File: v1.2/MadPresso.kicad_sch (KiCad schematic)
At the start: 42 parts, among them J1 Conn_01x07, J2 Conn_01x03, J3 Conn_01x02, J4 Conn_01x04, Q1 BC847, Q2 BSS84, U1 LTV-356T, U2 ADC101C021CIMK, U3 WeMos_D1_mini

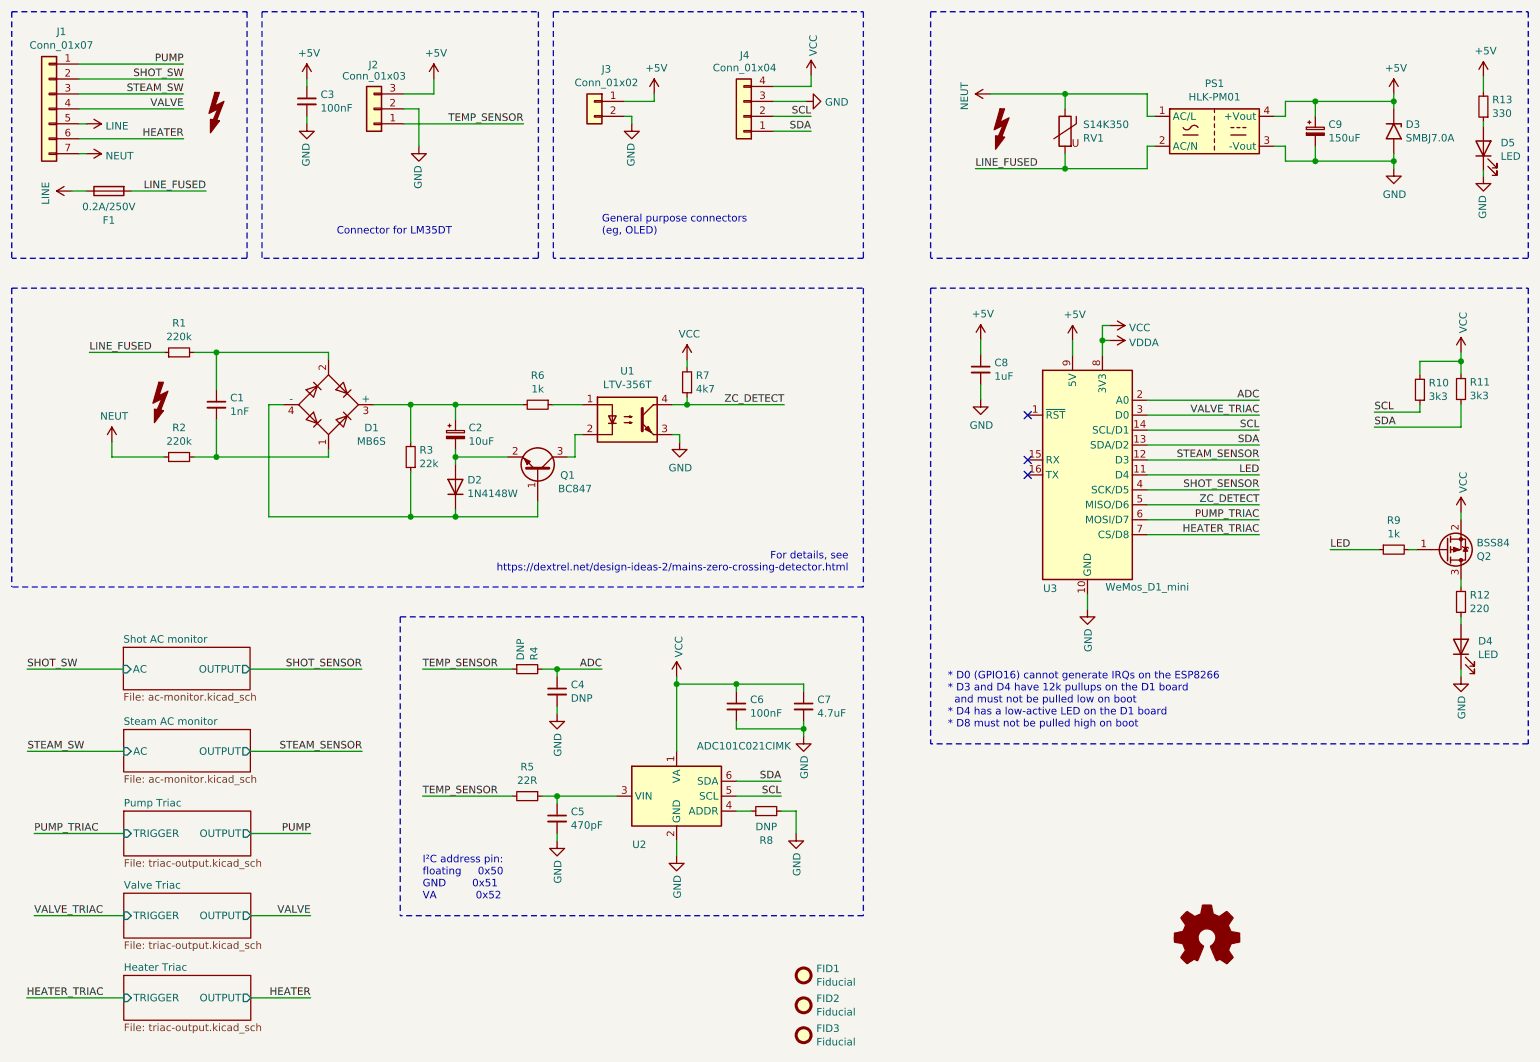
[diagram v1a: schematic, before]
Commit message: More updates
* make pump triac switch NEUT, not LINE
* move ADC a bit
* improve clearance
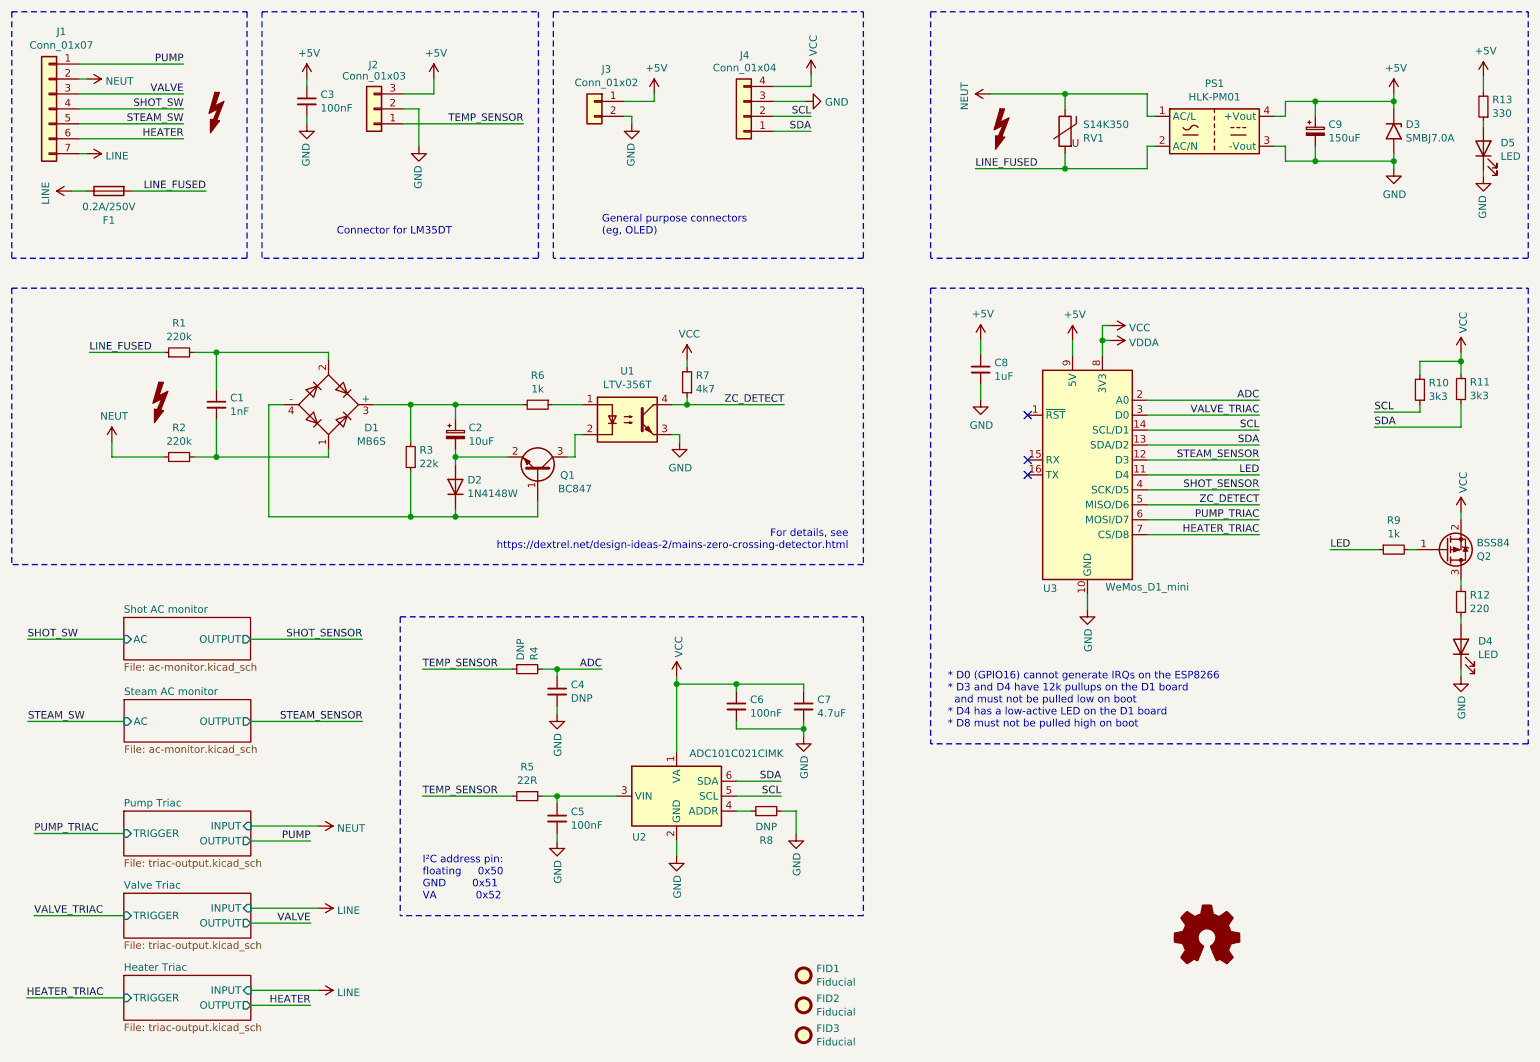
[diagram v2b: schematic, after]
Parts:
- C5: value 470pF -> 100nF
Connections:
- net LINE: now also J1.7 (Pin_7); no longer J1.5 (Pin_5)
- net NEUT: now also J1.2 (Pin_2); no longer J1.7 (Pin_7)
- net SHOT_SW: now also J1.4 (Pin_4); no longer J1.2 (Pin_2)
- net STEAM_SW: now also J1.5 (Pin_5); no longer J1.3 (Pin_3)
- net VALVE: now also J1.3 (Pin_3); no longer J1.4 (Pin_4)
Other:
- sheet Heater Triac ports: added INPUT; removed none
- sheet Pump Triac ports: added INPUT; removed none
- sheet Valve Triac ports: added INPUT; removed none

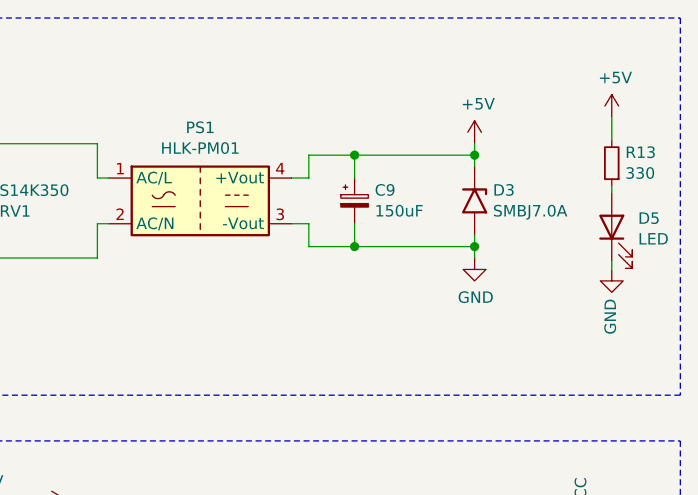
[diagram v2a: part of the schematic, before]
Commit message: more cleanups, replace caps with ceramic types, polygon updates
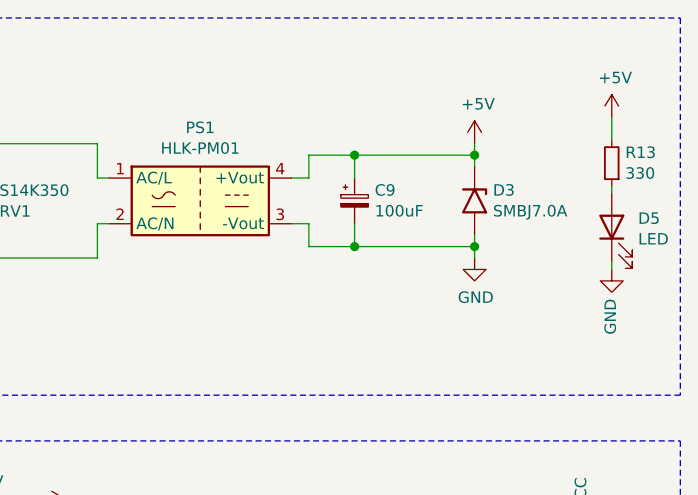
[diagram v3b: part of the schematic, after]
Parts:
- C2: footprint Capacitor_SMD:CP_Elec_4x5.8 -> Capacitor_Tantalum_SMD:CP_EIA-1608-08_AVX-J; symbol Device:CP_Small -> Device:C_Polarized_Small
- C9: value 150uF -> 100uF; footprint Capacitor_SMD:CP_Elec_8x10 -> Capacitor_Tantalum_SMD:CP_EIA-3216-18_Kemet-A_Pad1.58x1.35mm_HandSolder; symbol Device:CP_Small -> Device:C_Polarized_Small
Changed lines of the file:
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@@
   (junction (at 255.27 41.91) (diameter 1.016) (color 0 0 0 0))
   (junction (at 266.7 75.946) (diameter 1.016) (color 0 0 0 0))
+  (no_connect (at 193.04 95.25))
   (no_connect (at 193.04 92.71))
   (no_connect (at 193.04 85.09))
-  (no_connect (at 193.04 95.25))
   (wire (pts (xy 22.86 184.15) (xy 39.37 184.15))
     (stroke (width 0) (type solid) (color 0 0 0 0))
@@
     )
   )
-  (symbol (lib_id "Device:CP_Small") (at 95.758 88.392 0) (unit 1)
+  (symbol (lib_id "Device:C_Polarized_Small") (at 95.758 88.392 0) (unit 1)
     (in_bom yes) (on_board yes)
     (property "Reference" "C2" (id 0) (at 97.9932 87.2236 0)
@@
       (effects (font (size 1.27 1.27)) (justify left))
     )
-    (property "Footprint" "Capacitor_SMD:CP_Elec_4x5.8" (id 2) (at 95.758 88.392 0)
+    (property "Footprint" "Capacitor_Tantalum_SMD:CP_EIA-1608-08_AVX-J" (id 2) (at 95.758 88.392 0)
       (effects (font (size 1.27 1.27)) hide)
     )
@@
     )
   )
-  (symbol (lib_id "Device:CP_Small") (at 241.935 36.83 0) (unit 1)
+  (symbol (lib_id "Device:C_Polarized_Small") (at 241.935 36.83 0) (unit 1)
     (in_bom yes) (on_board yes)
     (property "Reference" "C9" (id 0) (at 244.1702 35.6616 0)
       (effects (font (size 1.27 1.27)) (justify left))
     )
-    (property "Value" "150uF" (id 1) (at 244.1702 37.973 0)
-      (effects (font (size 1.27 1.27)) (justify left))
-    )
-    (property "Footprint" "Capacitor_SMD:CP_Elec_8x10" (id 2) (at 241.935 36.83 0)
+    (property "Value" "100uF" (id 1) (at 244.1702 37.973 0)
+      (effects (font (size 1.27 1.27)) (justify left))
+    )
+    (property "Footprint" "Capacitor_Tantalum_SMD:CP_EIA-3216-18_Kemet-A_Pad1.58x1.35mm_HandSolder" (id 2) (at 241.935 36.83 0)
       (effects (font (size 1.27 1.27)) hide)
     )
@@
     )
     (path "/00000000-0000-0000-0000-00005fa76f4d"
-      (reference "C2") (unit 1) (value "10uF") (footprint "Capacitor_SMD:CP_Elec_4x5.8")
+      (reference "C2") (unit 1) (value "10uF") (footprint "Capacitor_Tantalum_SMD:CP_EIA-1608-08_AVX-J")
     )
     (path "/0bbd1c40-b800-4190-b61b-fff21288cdfd"
@@
     )
     (path "/00000000-0000-0000-0000-00005f9a3c16"
-      (reference "C9") (unit 1) (value "150uF") (footprint "Capacitor_SMD:CP_Elec_8x10")
+      (reference "C9") (unit 1) (value "100uF") (footprint "Capacitor_Tantalum_SMD:CP_EIA-3216-18_Kemet-A_Pad1.58x1.35mm_HandSolder")
     )
     (path "/525282e4-3a4c-4a30-9069-3bf74e46a09e"

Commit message: switch to ceramic caps
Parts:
- C2: footprint Capacitor_Tantalum_SMD:CP_EIA-1608-08_AVX-J -> Capacitor_SMD:C_0603_1608Metric_Pad1.08x0.95mm_HandSolder
- C9: footprint Capacitor_Tantalum_SMD:CP_EIA-3216-18_Kemet-A_Pad1.58x1.35mm_HandSolder -> Capacitor_SMD:C_1206_3216Metric_Pad1.33x1.80mm_HandSolder
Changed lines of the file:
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@@
   (junction (at 255.27 41.91) (diameter 1.016) (color 0 0 0 0))
   (junction (at 266.7 75.946) (diameter 1.016) (color 0 0 0 0))
+  (no_connect (at 193.04 85.09))
+  (no_connect (at 193.04 92.71))
   (no_connect (at 193.04 95.25))
-  (no_connect (at 193.04 92.71))
-  (no_connect (at 193.04 85.09))
   (wire (pts (xy 22.86 184.15) (xy 39.37 184.15))
     (stroke (width 0) (type solid) (color 0 0 0 0))
@@
       (effects (font (size 1.27 1.27)) (justify left))
     )
-    (property "Footprint" "Capacitor_Tantalum_SMD:CP_EIA-1608-08_AVX-J" (id 2) (at 95.758 88.392 0)
+    (property "Footprint" "Capacitor_SMD:C_0603_1608Metric_Pad1.08x0.95mm_HandSolder" (id 2) (at 95.758 88.392 0)
       (effects (font (size 1.27 1.27)) hide)
     )
@@
       (effects (font (size 1.27 1.27)) (justify left))
     )
-    (property "Footprint" "Capacitor_Tantalum_SMD:CP_EIA-3216-18_Kemet-A_Pad1.58x1.35mm_HandSolder" (id 2) (at 241.935 36.83 0)
+    (property "Footprint" "Capacitor_SMD:C_1206_3216Metric_Pad1.33x1.80mm_HandSolder" (id 2) (at 241.935 36.83 0)
       (effects (font (size 1.27 1.27)) hide)
     )
@@
     )
     (path "/00000000-0000-0000-0000-00005fa76f4d"
-      (reference "C2") (unit 1) (value "10uF") (footprint "Capacitor_Tantalum_SMD:CP_EIA-1608-08_AVX-J")
+      (reference "C2") (unit 1) (value "10uF") (footprint "Capacitor_SMD:C_0603_1608Metric_Pad1.08x0.95mm_HandSolder")
     )
     (path "/0bbd1c40-b800-4190-b61b-fff21288cdfd"
@@
     )
     (path "/00000000-0000-0000-0000-00005f9a3c16"
-      (reference "C9") (unit 1) (value "100uF") (footprint "Capacitor_Tantalum_SMD:CP_EIA-3216-18_Kemet-A_Pad1.58x1.35mm_HandSolder")
+      (reference "C9") (unit 1) (value "100uF") (footprint "Capacitor_SMD:C_1206_3216Metric_Pad1.33x1.80mm_HandSolder")
     )
     (path "/525282e4-3a4c-4a30-9069-3bf74e46a09e"
